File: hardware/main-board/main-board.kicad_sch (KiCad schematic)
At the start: 98 parts, among them J1 USB_C_Receptacle_USB2.0, J2 DNI, J3 Display Connector, J4 Conn_01x04, SW1 SW_Push, SW2 SW_Push, SW3 SW_Push, SW4 SW_Push, SW5 SW_Detect, SW6 SW_Boot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

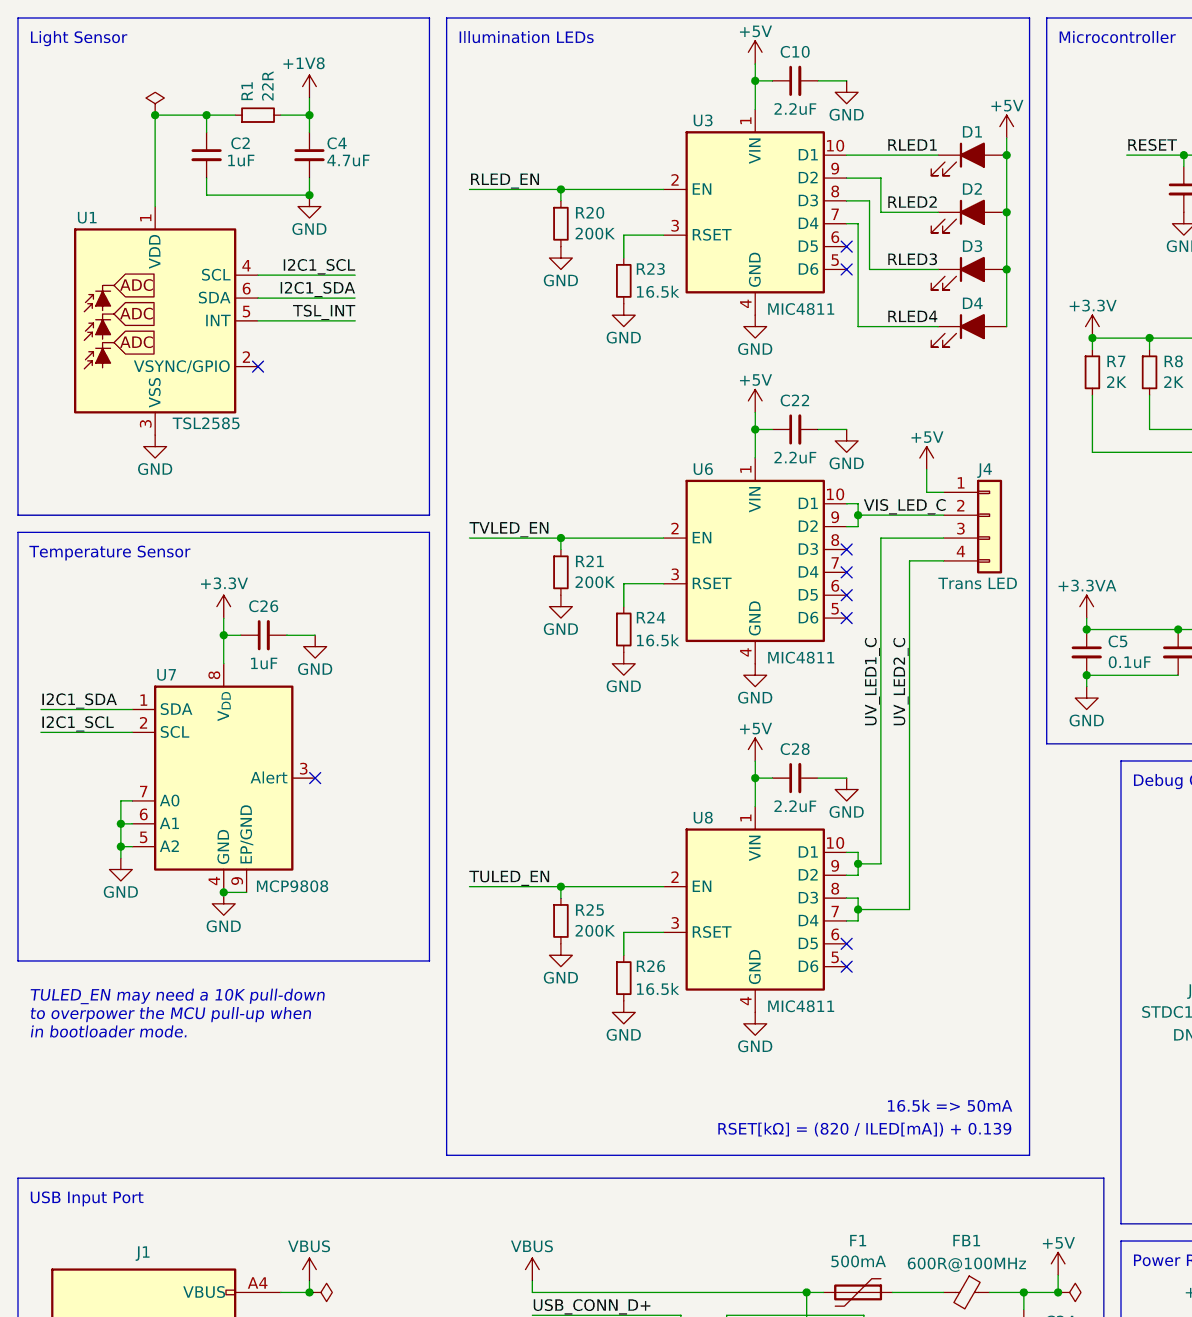
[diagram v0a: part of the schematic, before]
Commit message: Update main board for new transmission board interface
Removed the two transmission LED drivers from the main board, and routed
straight to the connecter per the new pinout.
Added a 10K pull-down to deal with the bootloader pin behavior issue.
Changed the reflection driver to the MIC4812, for part commonality and
slightly better thermals.
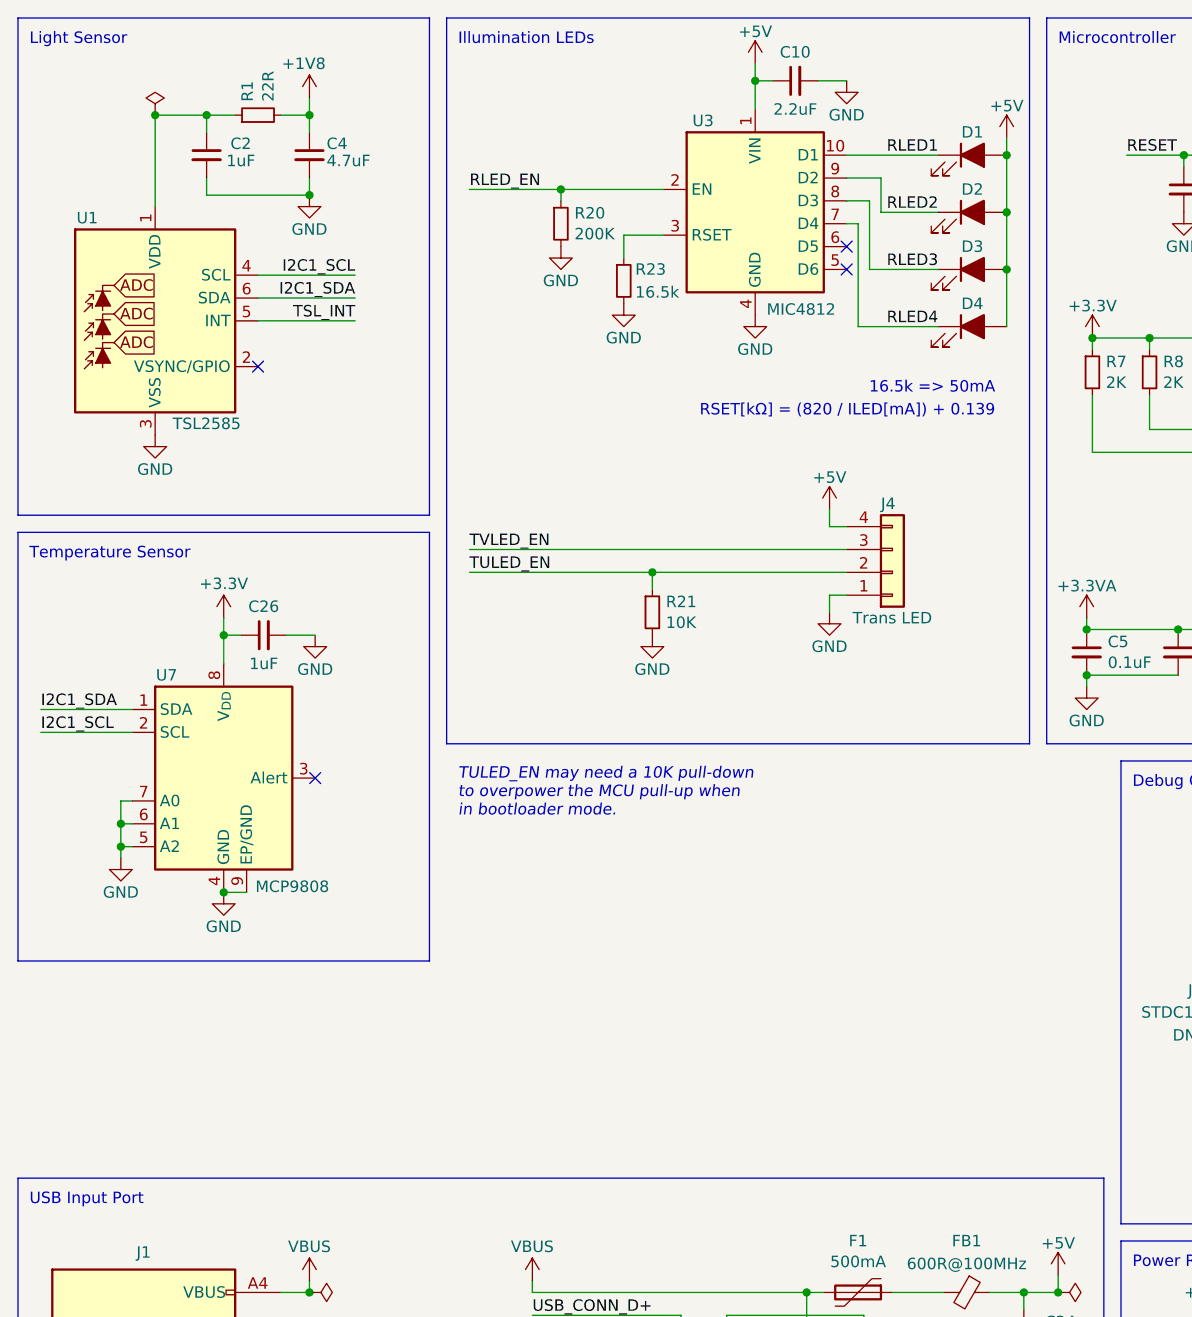
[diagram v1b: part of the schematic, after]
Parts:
- removed C22, C28: 2.2uF, Capacitor_SMD:C_0603_1608Metric, symbol Device:C_Small
- removed R24, R26: 16.5k, Resistor_SMD:R_0603_1608Metric, symbol Device:R_Small
- removed R25: 200K, Resistor_SMD:R_0603_1608Metric, symbol Device:R_Small
- removed U6, U8: MIC4811, Package_SO:MSOP-10_3x3mm_P0.5mm, symbol Project:MIC4811
- R21: value 200K -> 10K; Manufacturer TE Connectivity -> Yaego; Manufacturer PN CPF0603F200KC1 -> RC0603JR-0710KL; Supplier Digi-Key -> LCSC; Supplier PN A102235CT-ND -> C99198
- U3: value MIC4811 -> MIC4812; footprint Package_SO:MSOP-10_3x3mm_P0.5mm -> lib_fp:Micrel_MSOP-10-1EP_3x3mm_P0.5mm_EP1.73x1.7mm_ThermalVias; symbol Project:MIC4811 -> Project:MIC4812; Manufacturer PN MIC4811YMM -> MIC4812YMME; Supplier Digi-Key -> Mouser; Supplier PN 576-3858-5-ND -> 998-MIC4812YMME
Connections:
- net UV_LED1_C is gone; now on net TVLED_EN: J4.3 (Pin_3)
- net UV_LED2_C is gone; now on net +5V: J4.4 (Pin_4)
- net VIS_LED_C is gone; now on net TULED_EN: J4.2 (Pin_2)
- net +5V: no longer J4.1 (Pin_1)
- net GND: now also J4.1 (Pin_1), U3.11 (EP)
- net TULED_EN: now also R21.1
- net TVLED_EN: no longer R21.1
- no-connect marks 21 -> 15
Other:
- moved on the sheet: J4

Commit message: Prepare Rev B for the fab
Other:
- note added: "TULED_EN needs a 10K pull-down to overpower the MCU pull-up when in bootloader mode."
- note removed: "TULED_EN may need a 10K pull-down to overpower the MCU pull-up when in bootloader mode."
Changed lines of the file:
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@@
   (title_block
     (title "Printalyzer UV/VIS Densitometer - Main Board")
-    (date "2023-09-21")
+    (date "2023-11-27")
     (rev "B")
     (company "Dektronics, Inc.")
@@
     (effects (font (size 1.27 1.27)) (justify left bottom))
   )
-  (text "TULED_EN may need a 10K pull-down\nto overpower the MCU pull-up when\nin bootloader mode."
-    (at 63.5 103.505 0)
+  (text "TULED_EN needs a 10K pull-down to overpower\nthe MCU pull-up when in bootloader mode."
+    (at 62.865 94.615 0)
     (effects (font (size 1.27 1.27) italic) (justify left bottom))
   )
